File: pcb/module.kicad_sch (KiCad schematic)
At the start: 22 parts

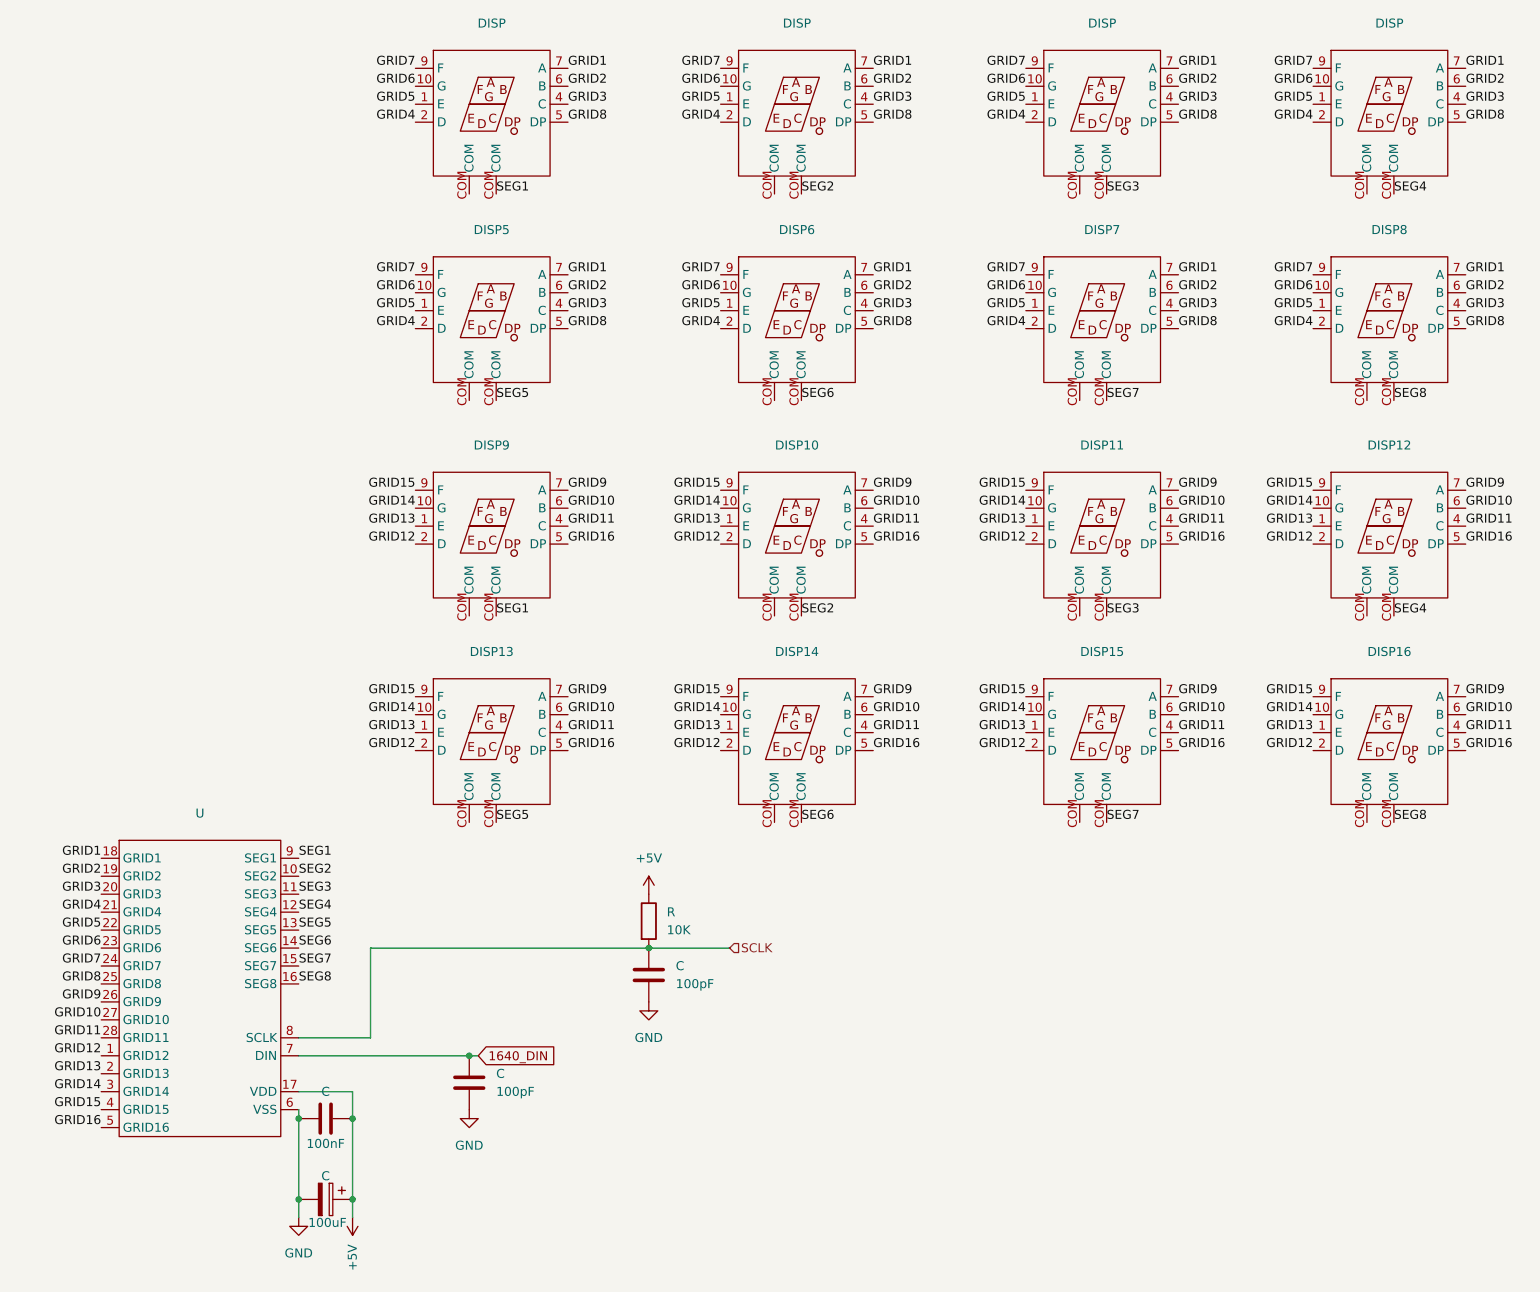
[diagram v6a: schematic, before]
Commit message: remove unneeded caps and pullups
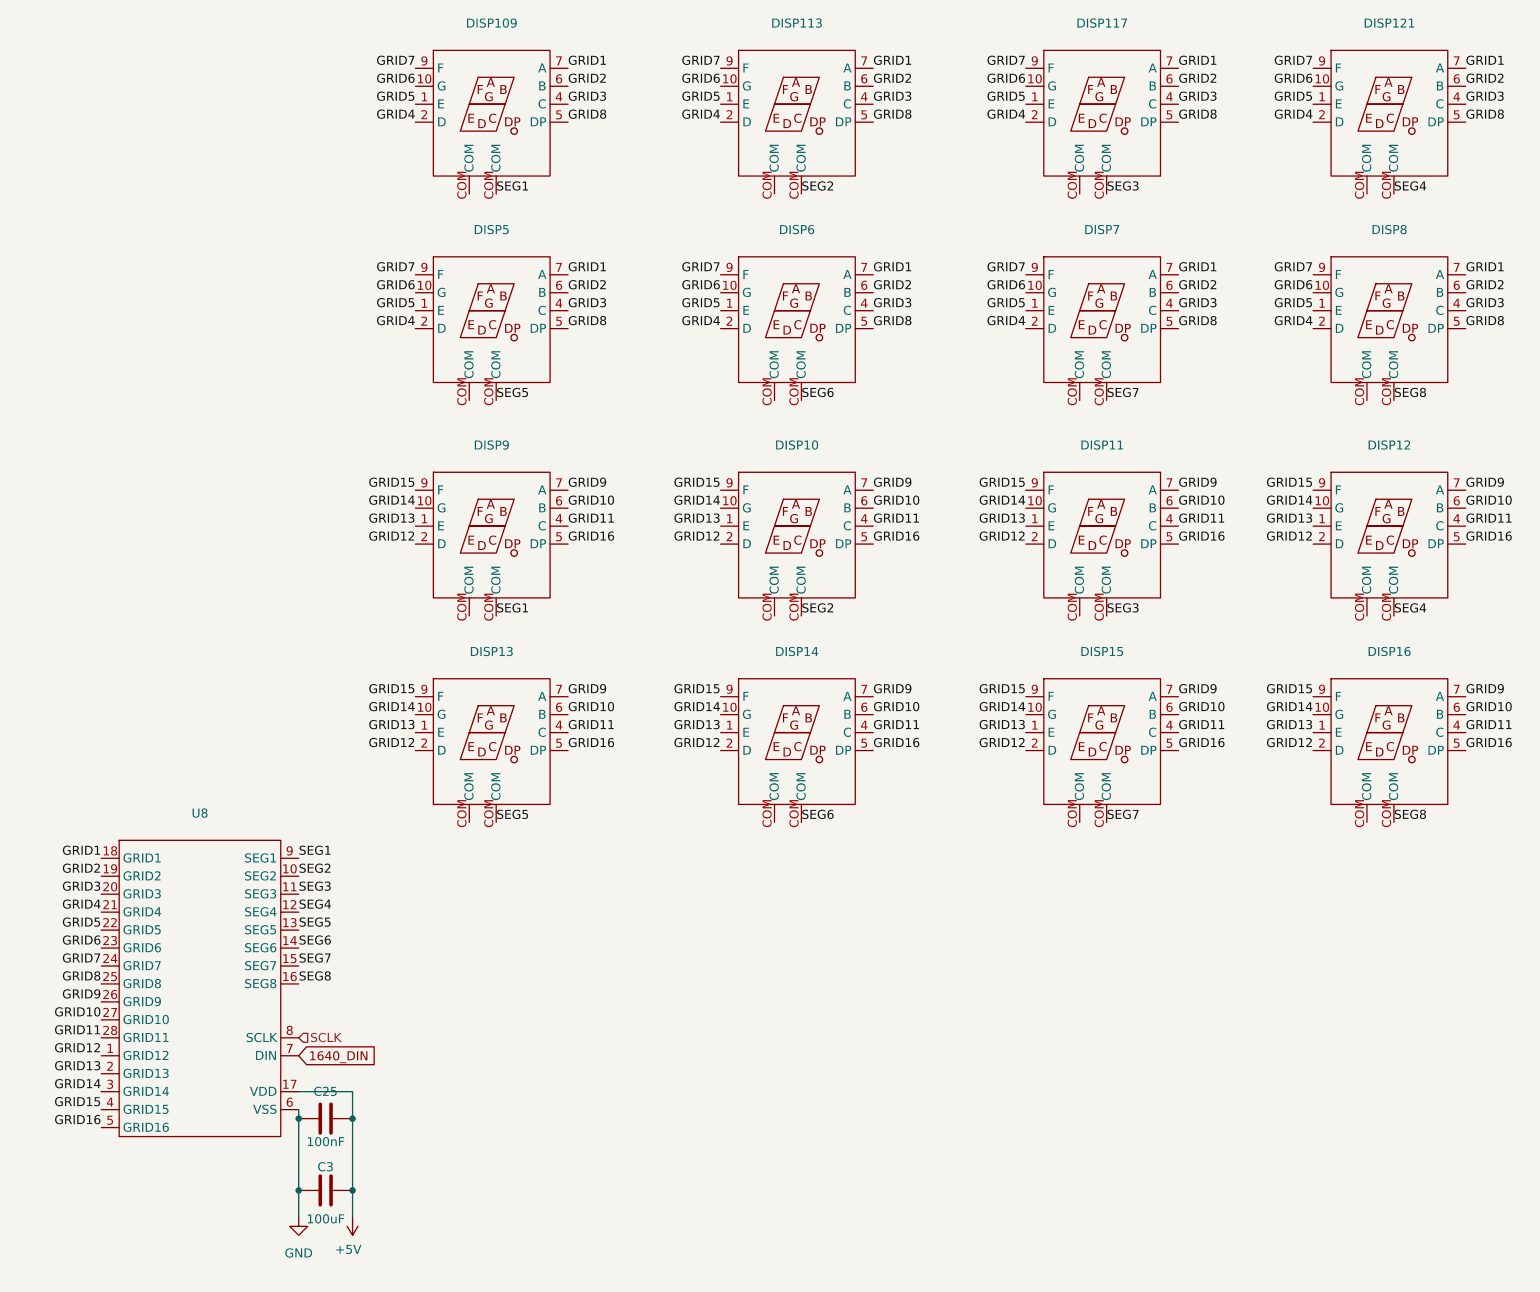
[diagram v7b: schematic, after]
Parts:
- removed C (x2): 100pF, symbol Device:C
- removed C: 100uF, symbol Device:C_Polarized
- removed R: 10K, symbol Device:R
- added C3: 100uF, symbol Device:C
- renumbered C to C25, DISP to DISP109, DISP to DISP113, DISP to DISP117, DISP to DISP121, U to U8
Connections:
- net +5V: now also C3.2
- net GND: now also C3.1

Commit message: switch to SSOP-28 for TM1640s
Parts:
- U8: footprint Package_SO:SOP-28_8.4x18.16mm_P1.27mm -> Package_SO:SSOP-28_3.9x9.9mm_P0.635mm
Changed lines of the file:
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@@
 			)
 		)
-		(property "Footprint" "Package_SO:SOP-28_8.4x18.16mm_P1.27mm"
+		(property "Footprint" "Package_SO:SSOP-28_3.9x9.9mm_P0.635mm"
 			(at -7.62 162.56 0)
 			(effects
